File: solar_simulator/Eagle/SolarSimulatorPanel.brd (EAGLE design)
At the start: 152 x 70 mm, 136 parts, among them J1 PJ-102B, J2 RAPC722BKZ-TH

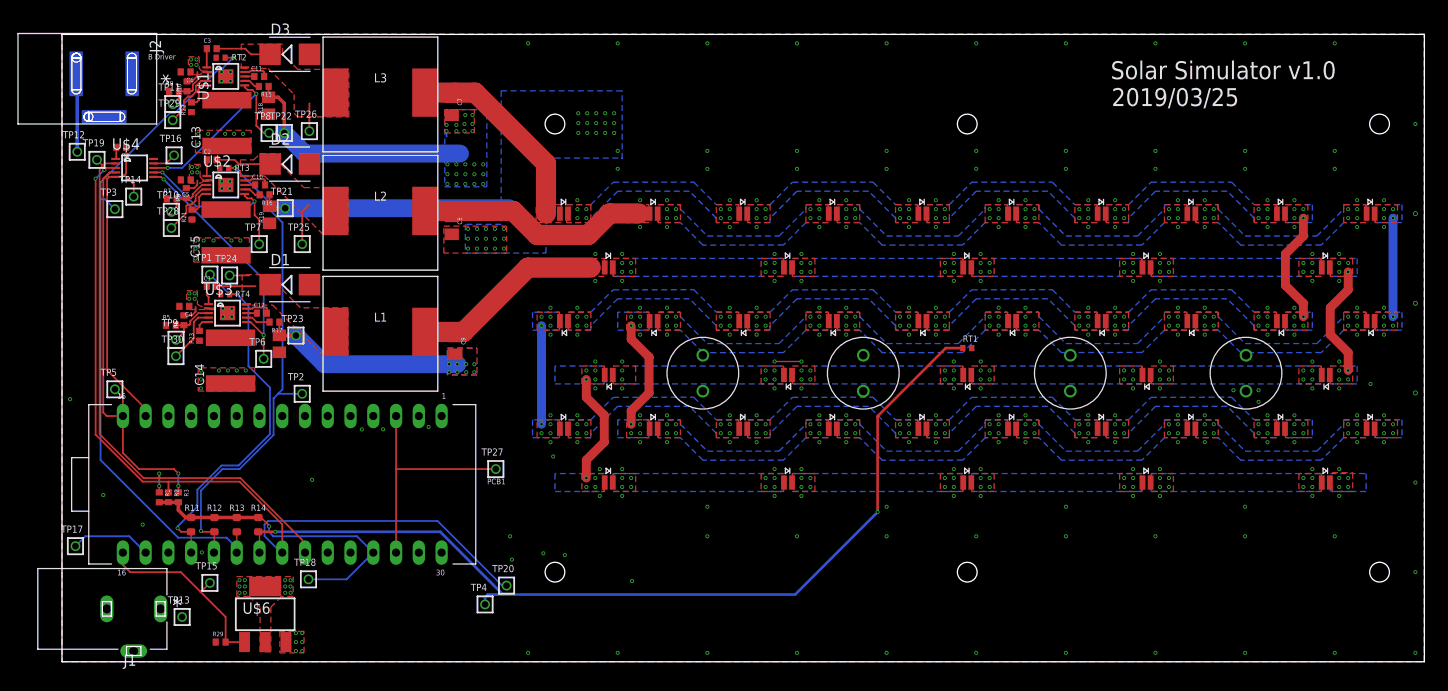
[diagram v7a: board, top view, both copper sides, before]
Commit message: revisions for solar simulator 2.0, removed outdated solarsim.lbr, new parts in oresat-eagle repo
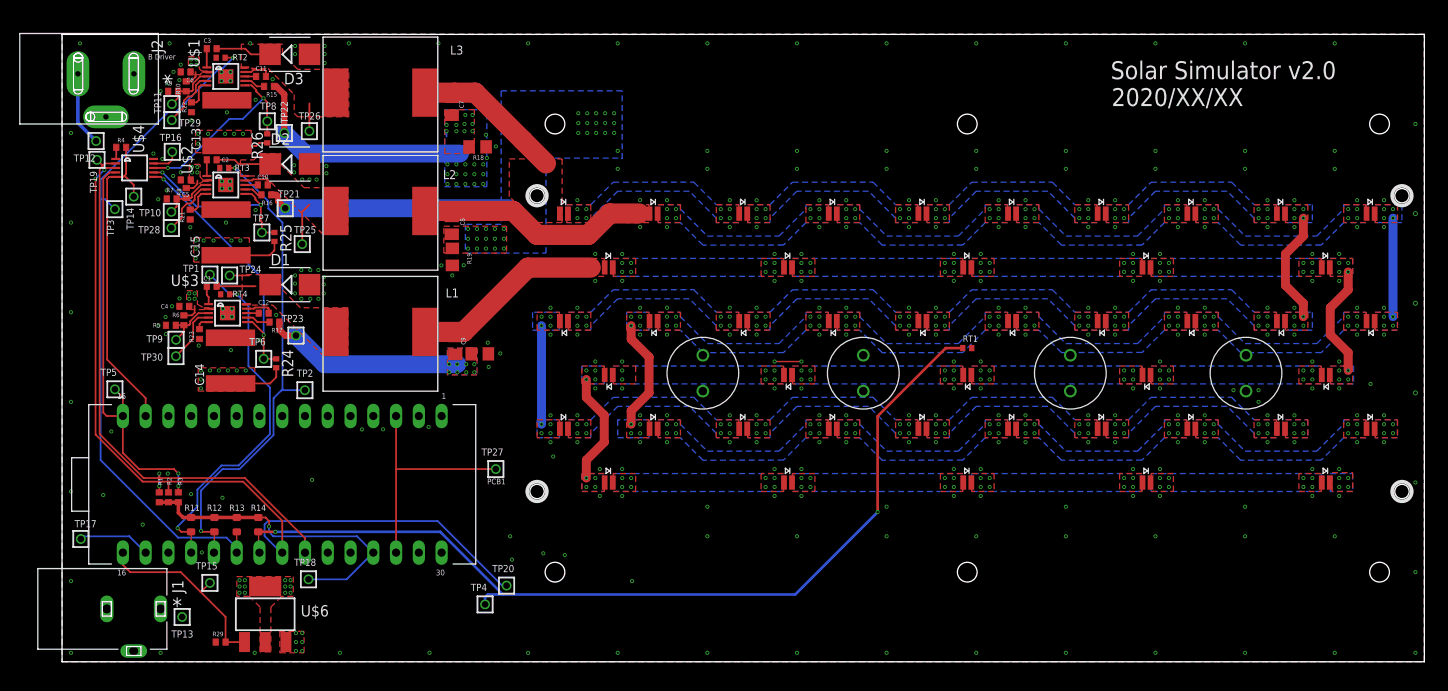
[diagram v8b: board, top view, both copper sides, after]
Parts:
- added R24, R25, R26: 10M, rcl:R0402
- R15, R16, R17: value TBD -> 1k
- moved R18 23.8 mm to (44.4, 57.5), turned to 180 degrees
- moved R20 22.4 mm to (44.6, 34.4), turned to 180 degrees
- moved R19 20.9 mm to (41.5, 45.2)
- moved TP12 2.42 mm to (1.80, 58.1)
- moved TP7 1.33 mm to (20.3, 47.9)
- moved TP8 1.32 mm to (20.9, 60.3)
- moved TP17 1.00 mm to (0.10, 13.7)
- moved R15 0.60 mm to (21.1, 64.2)
- moved TP2 0.50 mm to (25.1, 30.3)
- moved TP16 0.45 mm to (10.3, 56.9)
- moved C10 0.30 mm to (20.4, 53.2)
- moved R23 0.20 mm to (13.3, 36.6)
- moved J2 0.20 mm to (2.90, 65.6)
- moved C11 0.20 mm to (20.2, 65.3)
- moved C12 0.20 mm to (20.5, 38.9)
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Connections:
- net +3V3 renamed 3.3V
- net +5V renamed 5V
- net 56V: now also J2.P$2, R24.2, R25.2, R26.2; no longer J2.SLEEVE
- net GND: now also J2.P$1; no longer J2.CENTER
- net N$18: now also R25.1
- net N$64: now also R26.1
- net N$68: now also R24.1
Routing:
- net 56V: track 14.6 -> 31.8 mm, vias 32 -> 33
- net N$72: track 23.0 -> 17.4 mm
- net N$68: track 28.5 -> 29.9 mm
- net N$18: track 19.6 -> 20.5 mm
- net 3.3V: track 9.04 -> 8.11 mm
- net N$71: track 27.7 -> 27.0 mm
- net N$58: track 1.82 -> 2.42 mm
- net GND: track 12.7 -> 13.2 mm, vias 262 -> 341
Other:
- outline, holes or cut-outs redrawn
- board text added: "2020/XX/XX"
- board text added: "Solar Simulator v2.0"
- board text removed: "2019/03/25"
- board text removed: "Solar Simulator v1.0"
